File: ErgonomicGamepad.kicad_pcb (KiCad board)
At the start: 2 copper layers, 80 parts, among them J1 USB_C_Receptacle_USB2.0_16P, J2 Conn_01x08, J3 Conn_01x08, J4 Conn_01x08, J5 AVR-ISP-6, J6 Conn_01x08, J7 Conn_01x02, SW01 SW_DIP_x01, SW02 SW_DIP_x01, SW03 SW_DIP_x01, SW04 SW_DIP_x01, SW05 SW_DIP_x01, SW06 SW_DIP_x01, SW07 SW_DIP_x01, SW08 SW_DIP_x01, SW09 SW_DIP_x01, SW10 SW_DIP_x01, SW11 SW_DIP_x01, SW12 SW_DIP_x01, SW13 SW_DIP_x01, SW14 SW_DIP_x01, SW15 SW_DIP_x01, SW16 SW_DIP_x01, SW17 SW_DIP_x01, SW18 SW_DIP_x01, SW19 SW_DIP_x01, SW20 SW_DIP_x01, SW21 SW_DIP_x01, SW22 SW_DIP_x01, SW23 SW_DIP_x01, SW24 SW_DIP_x01, U1 ATmega32U4-A, Y1 Crystal

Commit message: chore: schematic runs ERC clean; parts need specification
Snapshot pin-remapping work plus JLC BOM tracking updates. Schematic
passes ERC with no errors, but most placed components still need
Manufacturer/MPN/Supplier/LCSC fields filled in (see
UnresolvedPartsPunchList.md for the full punch list).

Co-Authored-By: Claude Sonnet 5 <noreply@anthropic.com>
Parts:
- added U2: USBLC6-2SC6, Package_TO_SOT_SMD:SOT-23-6, F.Cu at (219.6, 47.4)
- D09, D10, D11, D12, D13, D14, D15, D16, D17, D18, D19, D2, D20, D21, D22, D23, D24, D3, D4, D5, D6, D7, D8: value 1N4148 -> 1N4148WS; footprint Diode_THT:D_DO-35_SOD27_P7.62mm_Horizontal -> Diode_SMD:D_SOD-323
- J5: footprint Connector_PinHeader_2.54mm:PinHeader_2x03_P2.54mm_Vertical -> Connector_PinHeader_2.54mm:PinHeader_2x03_P2.54mm_Vertical_SMD
- J7: value Conn_01x02 -> 1824417; footprint Connector_PinHeader_2.54mm:PinHeader_1x02_P2.54mm_Vertical -> Connector_Phoenix_MC_HighVoltage:PhoenixContact_MCV_1,5_2-G-5.08_1x02_P5.08mm_Vertical
- moved C1 287.0 mm to (109.3, 175.2)
- moved C5 287.0 mm to (113.3, 175.2)
- moved D1 287.0 mm to (130.8, 185.9)
- moved D10 287.0 mm to (98.2, 147.3)
- moved D11 287.0 mm to (98.2, 150.9)
- moved D15 287.0 mm to (98.2, 165.1)
- moved D16 287.0 mm to (98.2, 168.7)
- moved D18 287.0 mm to (109.0, 147.3)
- moved D19 287.0 mm to (109.0, 150.9)
- moved D2 287.0 mm to (87.5, 147.3)
- moved D23 287.0 mm to (109.0, 165.1)
- moved D24 287.0 mm to (109.0, 168.7)
- moved D3 287.0 mm to (87.5, 150.9)
- moved D7 287.0 mm to (87.5, 165.1)
- moved D8 287.0 mm to (87.5, 168.7)
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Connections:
- net Net-(D1-A) renamed /VBUS RAW
- R1 pad 1: Net-(J1-D--PadA7) -> Net-(R1-Pad1)
- R2 pad 1: Net-(J1-D+-PadA6) -> Net-(R2-Pad1)

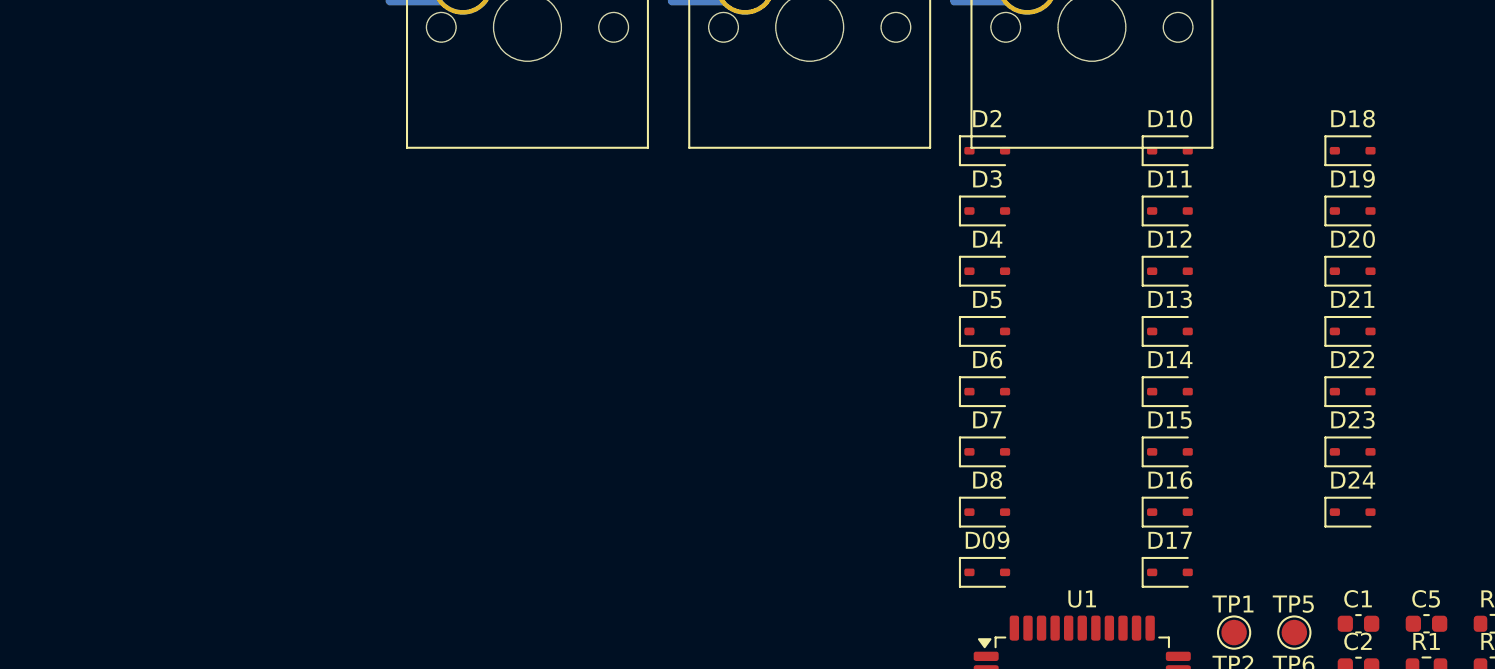
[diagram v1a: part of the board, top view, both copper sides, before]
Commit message: pcb: update from schematic after matrix diode renumbering
Sync footprint references (D2-D24 -> DM01-DM24) and part fields on the
PCB following the schematic-side matrix diode rename and LCSC part
backfill.

Co-Authored-By: Claude Sonnet 5 <noreply@anthropic.com>
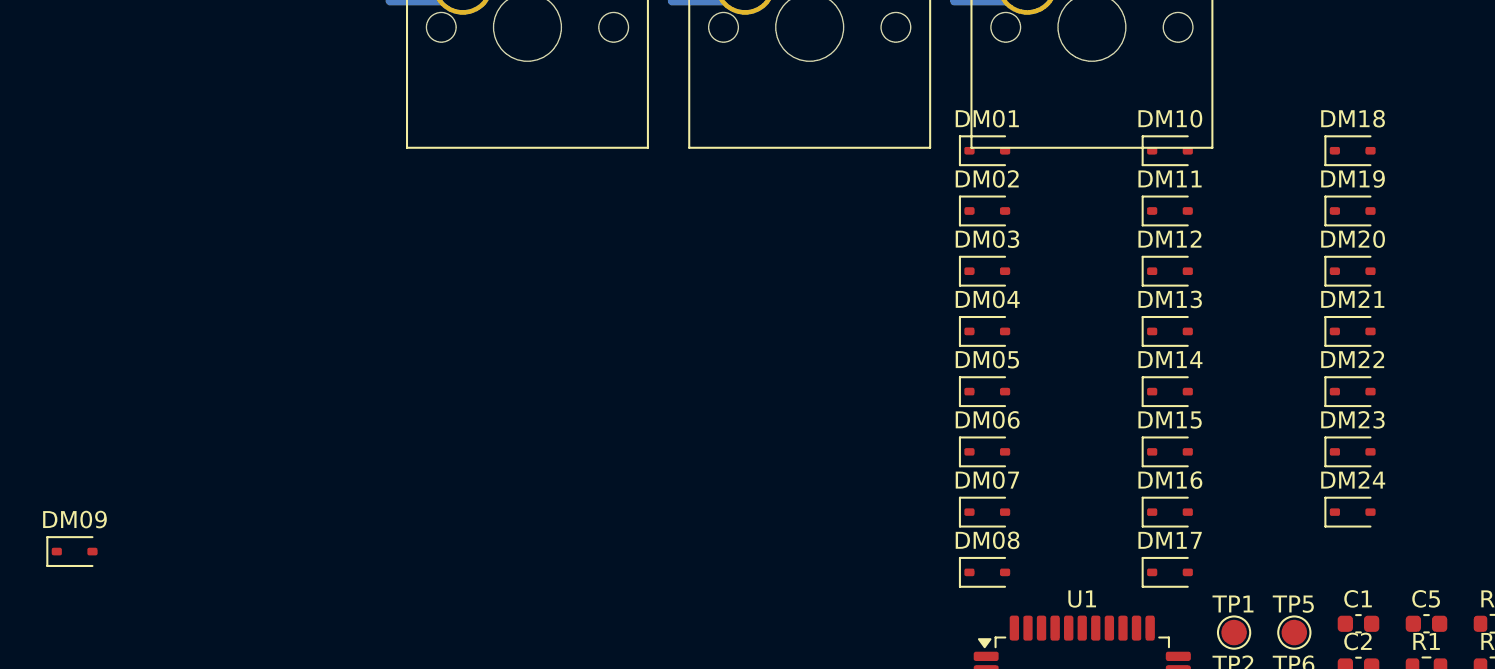
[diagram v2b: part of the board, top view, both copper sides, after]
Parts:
- added DM09: 1N4148WS, Diode_SMD:D_SOD-323, F.Cu at (33.7, 171.0)
- renumbered D2 to DM01, D3 to DM02, D4 to DM03, D5 to DM04, D6 to DM05, D7 to DM06, D8 to DM07, D09 to DM08, D10 to DM10, D11 to DM11, D12 to DM12, D13 to DM13, D14 to DM14, D15 to DM15, D16 to DM16, D17 to DM17, D18 to DM18, D19 to DM19, D20 to DM20, D21 to DM21, D22 to DM22, D23 to DM23, D24 to DM24
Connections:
- DM08 pad 1: /COL3 -> /COL2
- DM08 pad 2: Net-(D09-A) -> Net-(DM08-A)
- SW08 pad 2: Net-(D9-A) -> Net-(DM08-A)
- SW09 pad 2: Net-(D09-A) -> Net-(DM09-A)

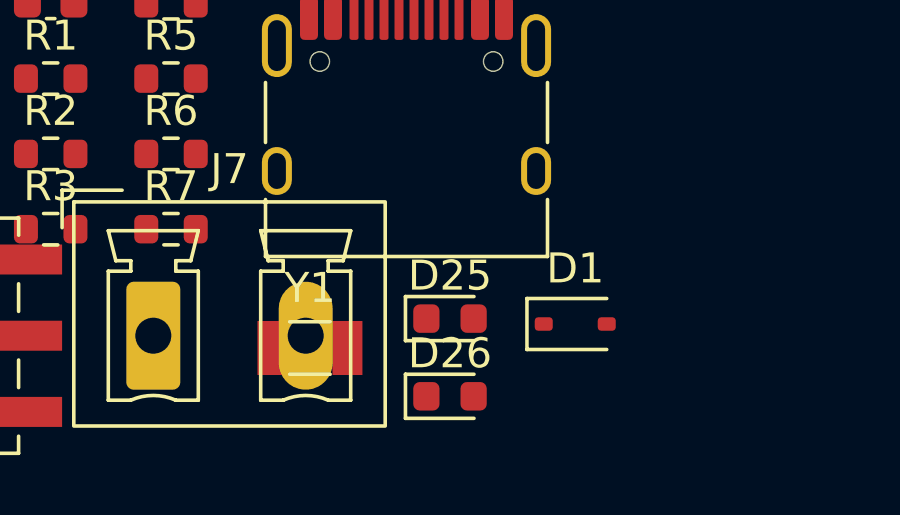
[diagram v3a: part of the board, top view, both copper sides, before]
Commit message: schematic+pcb: rename D25/D26 to LED1/LED2, specify parts
Rename the power and debug indicator LEDs to LED1/LED2 for clarity.
Backfill Manufacturer/MPN/LCSC/Datasheet: LED1 (Pwr, green) with
YONGYUTAI YLED0603G (LCSC C19273151), LED2 (Dbg, red) with Hubei
KENTO Elec KT-0603R (LCSC C2286). PCB updated from schematic to match.

Co-Authored-By: Claude Sonnet 5 <noreply@anthropic.com>
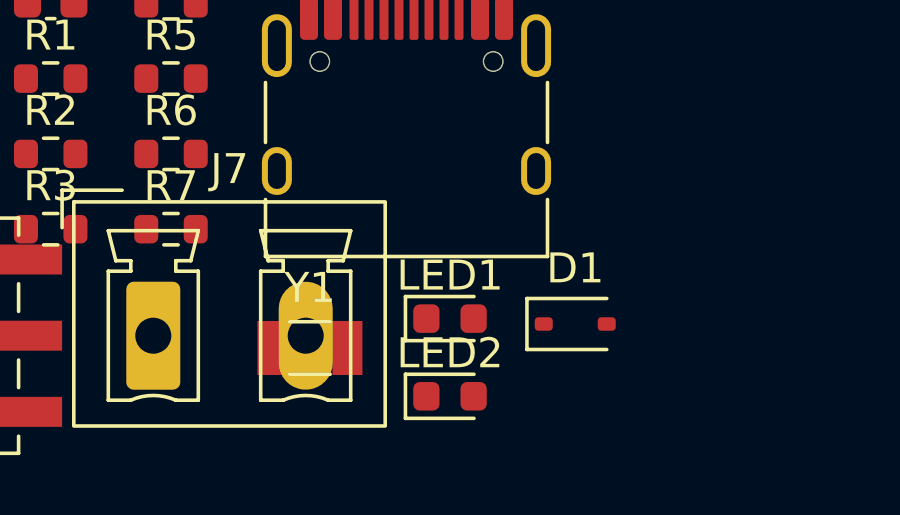
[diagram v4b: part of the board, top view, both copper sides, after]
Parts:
- renumbered D25 to LED1, D26 to LED2
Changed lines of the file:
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@@
 		(descr "LED SMD 0603 (1608 Metric), square (rectangular) end terminal, IPC-7351 nominal, (Body size source: http://www.tortai-tech.com/upload/download/2011102023233369053.pdf)")
 		(tags "LED")
-		(property "Reference" "D25"
+		(property "Reference" "LED1"
 			(at 0 -1.43 0)
 			(layer "F.SilkS")
@@
 			)
 		)
-		(property "Datasheet" ""
+		(property "Datasheet" "https://www.lcsc.com/datasheet/C19273151.pdf"
 			(at 0 0 0)
 			(layer "F.Fab")
@@
 			)
 		)
-		(property "Manufacturer" ""
+		(property "Manufacturer" "YONGYUTAI"
 			(at 0 0 0)
 			(unlocked yes)
@@
 			)
 		)
-		(property "MPN" ""
+		(property "MPN" "YLED0603G"
 			(at 0 0 0)
 			(unlocked yes)
@@
 			)
 		)
-		(property "LCSC" ""
+		(property "LCSC" "C19273151"
 			(at 0 0 0)
 			(unlocked yes)
@@
 			(layers "F.Cu" "F.Mask" "F.Paste")
 			(roundrect_rratio 0.25)
-			(net "Net-(D25-A)")
+			(net "Net-(LED1-A)")
 			(pinfunction "A_2")
 			(pintype "passive")
@@
 		(descr "LED SMD 0603 (1608 Metric), square (rectangular) end terminal, IPC-7351 nominal, (Body size source: http://www.tortai-tech.com/upload/download/2011102023233369053.pdf)")
 		(tags "LED")
-		(property "Reference" "D26"
+		(property "Reference" "LED2"
 			(at 0 -1.43 0)
 			(layer "F.SilkS")
@@
 			)
 		)
-		(property "Datasheet" ""
+		(property "Datasheet" "https://www.lcsc.com/datasheet/C2286.pdf"
 			(at 0 0 0)
 			(layer "F.Fab")
@@
 			)
 		)
-		(property "Manufacturer" ""
+		(property "Manufacturer" "Hubei KENTO Elec"
 			(at 0 0 0)
 			(unlocked yes)
@@
 			)
 		)
-		(property "MPN" ""
+		(property "MPN" "KT-0603R"
 			(at 0 0 0)
 			(unlocked yes)
@@
 			)
 		)
-		(property "LCSC" ""
+		(property "LCSC" "C2286"
 			(at 0 0 0)
 			(unlocked yes)
@@
 			(layers "F.Cu" "F.Mask" "F.Paste")
 			(roundrect_rratio 0.25)
-			(net "Net-(D26-A)")
+			(net "Net-(LED2-A)")
 			(pinfunction "A_2")
 			(pintype "passive")
@@
 			(layers "F.Cu" "F.Mask" "F.Paste")
 			(roundrect_rratio 0.25)
-			(net "Net-(D25-A)")
+			(net "Net-(LED1-A)")
 			(pintype "passive")
 		)
@@
 			(layers "F.Cu" "F.Mask" "F.Paste")
 			(roundrect_rratio 0.25)
-			(net "Net-(D26-A)")
+			(net "Net-(LED2-A)")
 			(pintype "passive")
 		)

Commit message: schematic+pcb: confirm U2 ESD part, add JP2 hardware bootloader jumper
U2 (USBLC6-2SC6): backfill LCSC C7519 and switch to LCSC-hosted
datasheet; verified via netlist trace that it's correctly wired to
the USB-C D+/D-/VBUS lines, confirming it's the right part for this
circuit.

JP1: convert from a solder jumper to a real 2-pin header
(Connector_PinHeader_2.54mm, Ckmtw B-2100S02P-A110 / LCSC C124375)
so a physical shunt can be inserted/removed by hand; flip it back to
a populated, in-BOM part.

JP2 (new): same physical-jumper header, wired to U1 pin 33
(PE2/HWB) and GND, so bridging it forces the ATmega32U4's hardware
DFU bootloader on reset. R8 (new, 10k) pulls PE2/HWB up to +5V so
the pin reads a clean high when JP2 isn't bridged, mirroring the
existing RESET/R3/SWR1 pattern.

Connectivity verified via netlist re-export and ERC (0
errors/warnings), including a scratch-copy test simulating both
jumpers bridged. Positions of JP2/R8 were manually adjusted in KiCad
after initial placement; PCB updated to match.

README updated: corrected the stale JP1 footprint entry and added a
note on sourcing 2.54mm jumper shunt caps (LCSC C5305), since JLCPCB
assembly solders the headers but not the removable shunts.

Co-Authored-By: Claude Sonnet 5 <noreply@anthropic.com>
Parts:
- added JP2: Jumper_2_Open, Connector_PinHeader_2.54mm:PinHeader_1x02_P2.54mm_Vertical, F.Cu at (-4.21, 76.8)
- added R8: 10k, Resistor_SMD:R_0603_1608Metric, F.Cu at (0.10, 75.8)
- JP1: value SolderJumper_2_Open -> Jumper_2_Open; footprint Jumper:SolderJumper-2_P1.3mm_Open_Pad1.0x1.5mm -> Connector_PinHeader_2.54mm:PinHeader_1x02_P2.54mm_Vertical
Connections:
- U1 pad 33: unconnected-(U1-~{HWB}/PE2-Pad33) -> /HWB
